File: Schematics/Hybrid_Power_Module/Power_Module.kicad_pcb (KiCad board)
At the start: 4 copper layers, 69.5 x 60 mm, 133 parts, among them J1 ScrewSwitch, J2 Battery, J3 ScrewSwitch, J4 GSE, J5 USB_C_Female_USB2_Small, J6 SWD_B, J7 Stack Male Edge Connector, Q1 AO4447A, Q2 SI2305CDS, Q3 DMN6040SSD-13, SW1 SW_STM_RESET, SW2 SW_STM_BOOT_MODE, U1 TPS61175PWPR, U10 LM66100DCKR, U11 LM66100DCKR, U12 AMS1117-3.3, U13 CP2102N-A02-GQFN20R, U14 STM32F103CBT6, U15 TCAN1051HGVDR, U16 BY25Q128ES, U2 LM74700QDBVRQ1, U3 LM74700QDBVRQ1, U4 ACS37041KLHBLT-010B3, U5 ACS37041KLHBLT-010B5, U6 INA187A, U7 LMR51430XDDCR, U8 LMR51430XDDCR, U9 LM66100DCKR, Y1 X322516MMB4SI

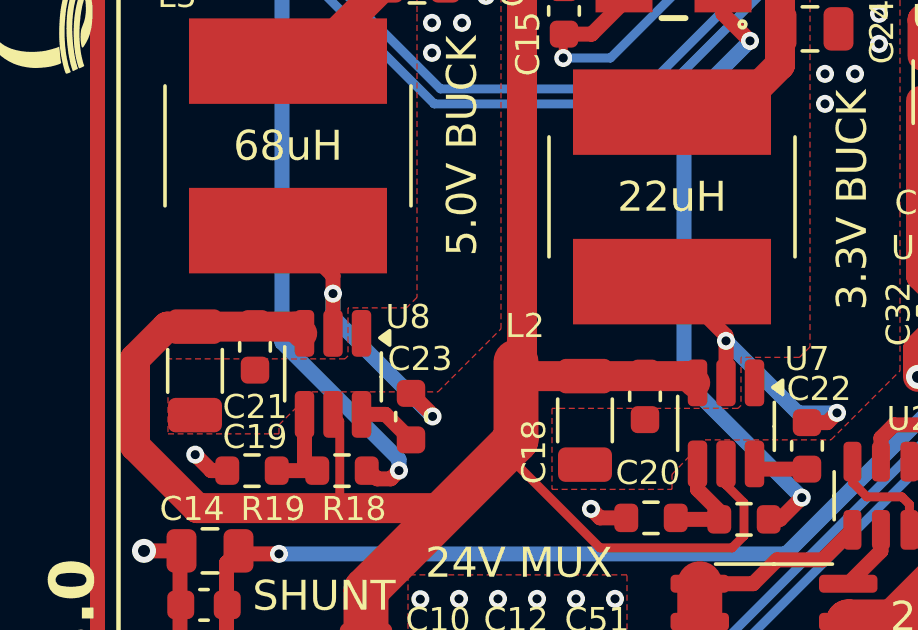
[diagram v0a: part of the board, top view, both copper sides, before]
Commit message: using copper poor for 5v and 3.3v buck sw
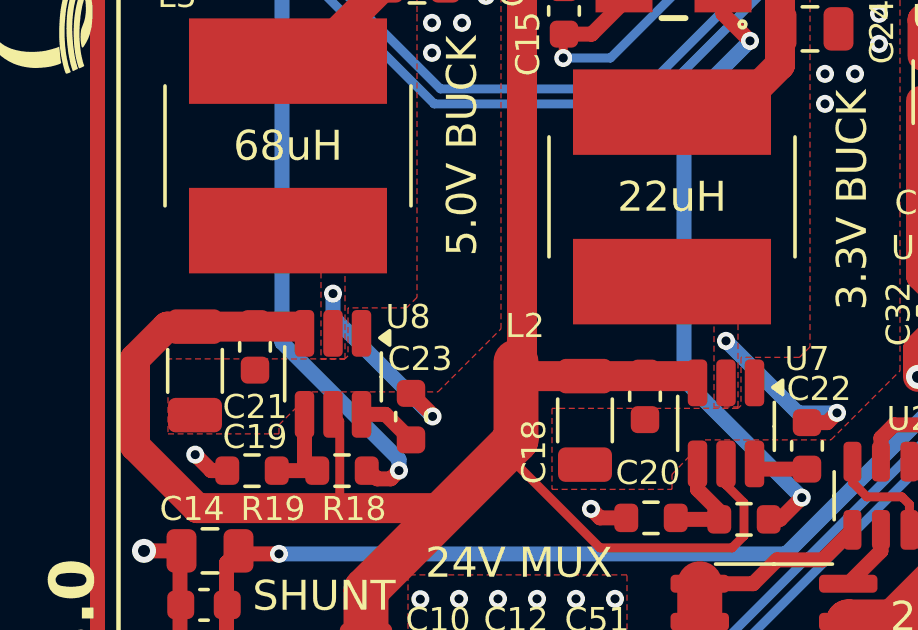
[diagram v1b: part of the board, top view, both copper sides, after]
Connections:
- net Net-(U7-SW) renamed /power/3.3V SW
- net Net-(U8-SW) renamed /power/5V SW
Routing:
- net /power/3.3V SW: track 9.95 -> 5.83 mm
- net /power/5V SW: track 10.6 -> 6.54 mm
- net 24V_MUX: track 94.7 -> 94.1 mm
- added copper zone on F.Cu, net /power/3.3V SW
- added copper zone on F.Cu, net /power/5V SW
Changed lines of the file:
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@@
 	(net 21 "CAN_TX")
 	(net 22 "Net-(C8-Pad1)")
-	(net 23 "Net-(U7-SW)")
+	(net 23 "/power/3.3V SW")
 	(net 24 "CAN_N")
 	(net 25 "CAN_P")
@@
 	(net 39 "MOSI_FL")
 	(net 40 "USART_TX")
-	(net 41 "Net-(U8-SW)")
+	(net 41 "/power/5V SW")
 	(net 42 "/power/GSE_SW+")
 	(net 43 "Net-(D5-A)")
@@
 			(size 6.6 2.85)
 			(layers "F.Cu" "F.Paste" "F.Mask")
-			(net 41 "Net-(U8-SW)")
+			(net 41 "/power/5V SW")
 			(pinfunction "1")
 			(pintype "passive")
@@
 			(layers "F.Cu" "F.Paste" "F.Mask")
 			(roundrect_rratio 0.25)
-			(net 41 "Net-(U8-SW)")
+			(net 41 "/power/5V SW")
 			(pinfunction "SW")
 			(pintype "power_in")
@@
 			(layers "F.Cu" "F.Paste" "F.Mask")
 			(roundrect_rratio 0.25)
-			(net 23 "Net-(U7-SW)")
+			(net 23 "/power/3.3V SW")
 			(pinfunction "SW")
 			(pintype "power_in")
@@
 			(layers "F.Cu" "F.Paste" "F.Mask")
 			(roundrect_rratio 0.25)
-			(net 23 "Net-(U7-SW)")
+			(net 23 "/power/3.3V SW")
 			(pintype "passive")
 		)
@@
 			(size 6.6 2.85)
 			(layers "F.Cu" "F.Paste" "F.Mask")
-			(net 23 "Net-(U7-SW)")
+			(net 23 "/power/3.3V SW")
 			(pinfunction "2")
 			(pintype "passive")
@@
 			(layers "F.Cu" "F.Paste" "F.Mask")
 			(roundrect_rratio 0.25)
-			(net 41 "Net-(U8-SW)")
+			(net 41 "/power/5V SW")
 			(pintype "passive")
 		)
@@
 	)
 	(segment
-		(start 155.25 67.275)
-		(end 155.475 67.5)
-		(width 1)
-		(layer "F.Cu")
-		(net 2)
-	)
-	(segment
-		(start 138.8 65.625)
-		(end 142.15 65.625)
-		(width 1)
-		(layer "F.Cu")
-		(net 2)
-	)
-	(segment
 		(start 154.4 48.3)
 		(end 153.4 48.3)
@@
 	)
 	(segment
+		(start 138.8 65.625)
+		(end 142.225 65.625)
+		(width 1)
+		(layer "F.Cu")
+		(net 2)
+	)
+	(segment
 		(start 157.1 71.5)
 		(end 157.1 72.6)
@@
 	)
 	(segment
-		(start 142.15 65.625)
-		(end 142.375 65.85)
-		(width 1)
-		(layer "F.Cu")
-		(net 2)
-	)
-	(segment
 		(start 142 76.6)
 		(end 141.7875 76.6)
@@
 	)
 	(segment
-		(start 156.5 66.1)
-		(end 156.5 65.925)
-		(width 0.5)
-		(layer "F.Cu")
-		(net 23)
-	)
-	(segment
 		(start 159.875 68.825)
 		(end 159.2 68.825)
@@
 		(net 23)
 	)
-	(segment
-		(start 156.5 67.5)
-		(end 156.5 66.1)
-		(width 0.5)
-		(layer "F.Cu")
-		(net 23)
-	)
-	(segment
-		(start 156.5 65.925)
-		(end 154.7 64.125)
-		(width 0.5)
-		(layer "F.Cu")
-		(net 23)
-	)
 	(via
 		(at 160.2 68.5)
@@
 	)
 	(segment
-		(start 143.4 64.525)
-		(end 143.4 63.925)
-		(width 0.5)
-		(layer "F.Cu")
-		(net 41)
-	)
-	(segment
 		(start 146.719764 68.618557)
 		(end 146.719764 68.569764)
@@
 	)
 	(segment
-		(start 143.4 63.925)
-		(end 141.9 62.425)
-		(width 0.5)
-		(layer "F.Cu")
-		(net 41)
-	)
-	(segment
 		(start 146.719764 68.569764)
 		(end 146 67.85)
@@
 		(net 41)
 	)
-	(segment
-		(start 143.4 65.85)
-		(end 143.4 64.525)
-		(width 0.5)
-		(layer "F.Cu")
-		(net 41)
-	)
 	(via
 		(at 143.4 64.525)
@@
 	)
 	(zone
+		(net 41)
+		(net_name "/power/5V SW")
+		(layer "F.Cu")
+		(hatch edge 0.5)
+		(priority 13)
+		(connect_pads yes
+			(clearance 0)
+		)
+		(min_thickness 0.25)
+		(filled_areas_thickness no)
+		(fill yes
+			(thermal_gap 0.5)
+			(thermal_bridge_width 0.5)
+		)
+		(polygon
+			(pts
+				(xy 143 66.7) (xy 143.8 66.7) (xy 143.8 63.5) (xy 143 63.5)
+			)
+		)
+	)
+	(zone
 		(net 1)
 		(net_name "GND")
@@
 			)
 		)
+	)
+	(zone
+		(net 23)
+		(net_name "/power/3.3V SW")
+		(layer "F.Cu")
+		(hatch edge 0.5)
+		(priority 14)
+		(connect_pads yes
+			(clearance 0)
+		)
+		(min_thickness 0.25)
+		(filled_areas_thickness no)
+		(fill yes
+			(thermal_gap 0.5)
+			(thermal_bridge_width 0.5)
+		)
+		(polygon
+			(pts
+				(xy 156.1 68.3) (xy 156.9 68.3) (xy 156.9 65.3) (xy 156.1 65.3)
+			)
+		)
